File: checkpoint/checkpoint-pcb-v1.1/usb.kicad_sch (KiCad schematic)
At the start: 7 parts, among them J16 USB_C_Receptacle_USB2.0_16P, U4 USBLC6-2P6

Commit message: chore: reset refdes numbers
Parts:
- renumbered J16 to J17
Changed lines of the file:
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@@
 		(dnp no)
 		(fields_autoplaced yes)
-		(property "Reference" "#PWR049"
+		(property "Reference" "#PWR051"
 			(at 151.13 58.42 0)
 			(effects
@@
 			(project "checkpoint"
 				(path "/3a22685f-fb6f-4c54-b509-09f3e7d2168e/d0edb953-abc9-4de2-ace2-d042dedd6b65"
-					(reference "#PWR049")
+					(reference "#PWR051")
 					(unit 1)
 				)
@@
 		(dnp no)
 		(fields_autoplaced yes)
-		(property "Reference" "#PWR051"
+		(property "Reference" "#PWR053"
 			(at 199.39 152.4 0)
 			(effects
@@
 			(project "checkpoint"
 				(path "/3a22685f-fb6f-4c54-b509-09f3e7d2168e/d0edb953-abc9-4de2-ace2-d042dedd6b65"
-					(reference "#PWR051")
+					(reference "#PWR053")
 					(unit 1)
 				)
@@
 		(on_board yes)
 		(dnp no)
-		(property "Reference" "J16"
+		(property "Reference" "J17"
 			(at 135.89 108.458 0)
 			(effects
@@
 			(project "checkpoint"
 				(path "/3a22685f-fb6f-4c54-b509-09f3e7d2168e/d0edb953-abc9-4de2-ace2-d042dedd6b65"
-					(reference "J16")
+					(reference "J17")
 					(unit 1)
 				)
@@
 		(dnp no)
 		(fields_autoplaced yes)
-		(property "Reference" "#PWR050"
+		(property "Reference" "#PWR052"
 			(at 158.75 58.42 0)
 			(effects
@@
 			(project "checkpoint"
 				(path "/3a22685f-fb6f-4c54-b509-09f3e7d2168e/d0edb953-abc9-4de2-ace2-d042dedd6b65"
-					(reference "#PWR050")
+					(reference "#PWR052")
 					(unit 1)
 				)
@@
 		(dnp no)
 		(fields_autoplaced yes)
-		(property "Reference" "#PWR046"
+		(property "Reference" "#PWR048"
 			(at 110.49 130.81 0)
 			(effects
@@
 			(project "checkpoint"
 				(path "/3a22685f-fb6f-4c54-b509-09f3e7d2168e/d0edb953-abc9-4de2-ace2-d042dedd6b65"
-					(reference "#PWR046")
+					(reference "#PWR048")
 					(unit 1)
 				)
@@
 		(dnp no)
 		(fields_autoplaced yes)
-		(property "Reference" "#PWR048"
+		(property "Reference" "#PWR050"
 			(at 147.32 144.78 0)
 			(effects
@@
 			(project "checkpoint"
 				(path "/3a22685f-fb6f-4c54-b509-09f3e7d2168e/d0edb953-abc9-4de2-ace2-d042dedd6b65"
-					(reference "#PWR048")
+					(reference "#PWR050")
 					(unit 1)
 				)
@@
 		(dnp no)
 		(fields_autoplaced yes)
-		(property "Reference" "#PWR047"
+		(property "Reference" "#PWR049"
 			(at 118.11 97.79 0)
 			(effects
@@
 			(project "checkpoint"
 				(path "/3a22685f-fb6f-4c54-b509-09f3e7d2168e/d0edb953-abc9-4de2-ace2-d042dedd6b65"
-					(reference "#PWR047")
+					(reference "#PWR049")
 					(unit 1)
 				)

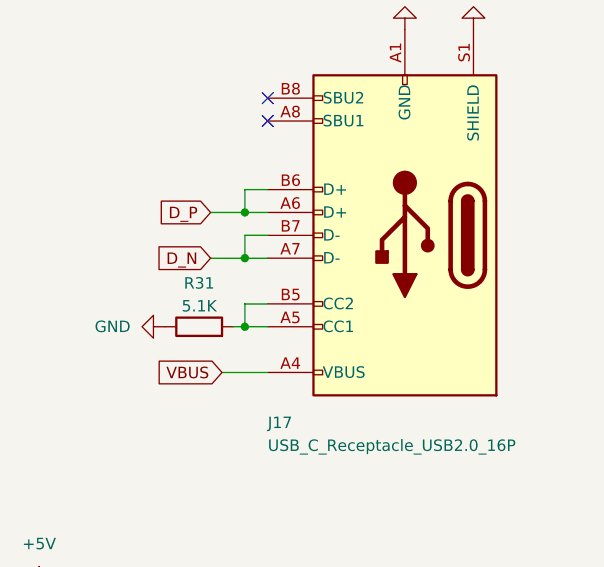
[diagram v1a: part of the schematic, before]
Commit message: fix: add i2c pullup resistors
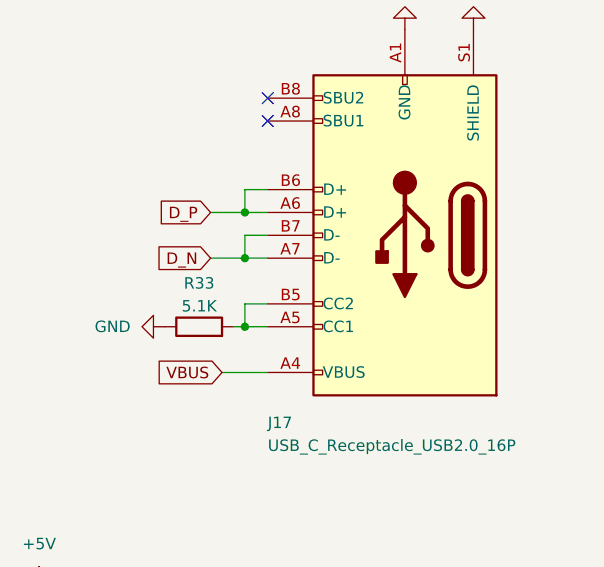
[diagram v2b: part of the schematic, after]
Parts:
- renumbered R31 to R33
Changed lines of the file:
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@@
 		(dnp no)
 		(fields_autoplaced yes)
-		(property "Reference" "#PWR051"
+		(property "Reference" "#PWR052"
 			(at 151.13 58.42 0)
 			(effects
@@
 			(project "checkpoint"
 				(path "/3a22685f-fb6f-4c54-b509-09f3e7d2168e/d0edb953-abc9-4de2-ace2-d042dedd6b65"
-					(reference "#PWR051")
+					(reference "#PWR052")
 					(unit 1)
 				)
@@
 		(dnp no)
 		(fields_autoplaced yes)
-		(property "Reference" "#PWR053"
+		(property "Reference" "#PWR054"
 			(at 199.39 152.4 0)
 			(effects
@@
 			(project "checkpoint"
 				(path "/3a22685f-fb6f-4c54-b509-09f3e7d2168e/d0edb953-abc9-4de2-ace2-d042dedd6b65"
-					(reference "#PWR053")
+					(reference "#PWR054")
 					(unit 1)
 				)
@@
 		(dnp no)
 		(fields_autoplaced yes)
-		(property "Reference" "#PWR052"
+		(property "Reference" "#PWR053"
 			(at 158.75 58.42 0)
 			(effects
@@
 			(project "checkpoint"
 				(path "/3a22685f-fb6f-4c54-b509-09f3e7d2168e/d0edb953-abc9-4de2-ace2-d042dedd6b65"
-					(reference "#PWR052")
+					(reference "#PWR053")
 					(unit 1)
 				)
@@
 		(dnp no)
 		(fields_autoplaced yes)
-		(property "Reference" "#PWR048"
+		(property "Reference" "#PWR049"
 			(at 110.49 130.81 0)
 			(effects
@@
 			(project "checkpoint"
 				(path "/3a22685f-fb6f-4c54-b509-09f3e7d2168e/d0edb953-abc9-4de2-ace2-d042dedd6b65"
-					(reference "#PWR048")
+					(reference "#PWR049")
 					(unit 1)
 				)
@@
 		(dnp no)
 		(fields_autoplaced yes)
-		(property "Reference" "#PWR050"
+		(property "Reference" "#PWR051"
 			(at 147.32 144.78 0)
 			(effects
@@
 			(project "checkpoint"
 				(path "/3a22685f-fb6f-4c54-b509-09f3e7d2168e/d0edb953-abc9-4de2-ace2-d042dedd6b65"
-					(reference "#PWR050")
+					(reference "#PWR051")
 					(unit 1)
 				)
@@
 		(dnp no)
 		(fields_autoplaced yes)
-		(property "Reference" "#PWR049"
+		(property "Reference" "#PWR050"
 			(at 118.11 97.79 0)
 			(effects
@@
 			(project "checkpoint"
 				(path "/3a22685f-fb6f-4c54-b509-09f3e7d2168e/d0edb953-abc9-4de2-ace2-d042dedd6b65"
-					(reference "#PWR049")
+					(reference "#PWR050")
 					(unit 1)
 				)
@@
 		(on_board yes)
 		(dnp no)
-		(property "Reference" "R31"
+		(property "Reference" "R33"
 			(at 128.27 92.964 90)
 			(effects
@@
 			(project "checkpoint"
 				(path "/3a22685f-fb6f-4c54-b509-09f3e7d2168e/d0edb953-abc9-4de2-ace2-d042dedd6b65"
-					(reference "R31")
+					(reference "R33")
 					(unit 1)
 				)

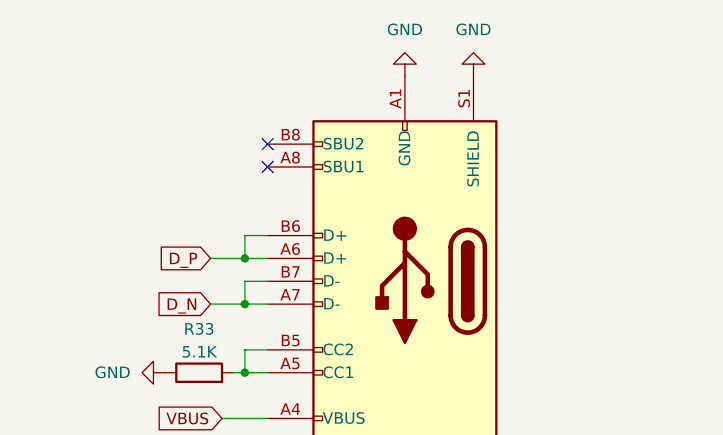
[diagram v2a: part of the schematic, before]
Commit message: chore: switch to vertical usb-c port
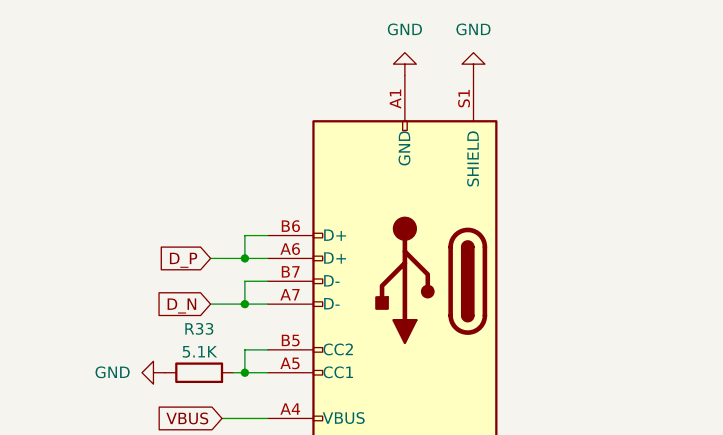
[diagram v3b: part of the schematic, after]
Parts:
- J17: footprint Connector_USB:USB_C_Receptacle_XKB_U262-16XN-4BVC11 -> Library:USB_C_14P_VERT_XUNPU; symbol Connector:USB_C_Receptacle_USB2.0_16P -> Connector:USB_C_Receptacle_USB2.0_14P
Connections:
- no-connect marks 2 -> 0
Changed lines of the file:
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@@
 		(color 0 0 0 0)
-	)
-	(no_connect
-		(at 135.89 72.39)
-	)
-	(no_connect
-		(at 135.89 74.93)
 	)
 	(wire
@@
 	)
 	(symbol
-		(lib_id "Connector:USB_C_Receptacle_USB2.0_16P")
+		(lib_id "Connector:USB_C_Receptacle_USB2.0_14P")
 		(at 151.13 87.63 180)
 		(unit 1)
@@
 			)
 		)
-		(property "Footprint" "Connector_USB:USB_C_Receptacle_XKB_U262-16XN-4BVC11"
+		(property "Footprint" "Library:USB_C_14P_VERT_XUNPU"
 			(at 147.32 87.63 0)
 			(effects
@@
 			)
 		)
-		(property "Description" "USB 2.0-only 16P Type-C Receptacle connector"
+		(property "Description" "USB 2.0-only 14P Type-C Receptacle connector"
 			(at 151.13 87.63 0)
 			(effects
@@
 		(pin "A9"
 		)
-		(pin "A8"
-		)
-		(pin "B8"
-		)
 		(instances

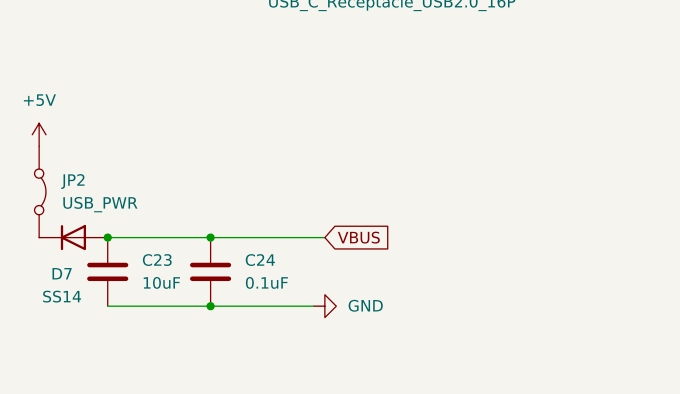
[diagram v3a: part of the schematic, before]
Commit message: chore: update component rotation
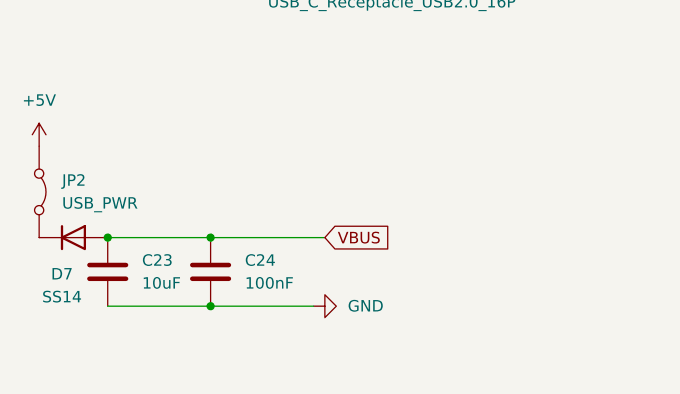
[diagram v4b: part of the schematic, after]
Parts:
- C24: value 0.1uF -> 100nF
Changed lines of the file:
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@@
 			)
 		)
-		(property "Value" "0.1uF"
+		(property "Value" "100nF"
 			(at 133.35 142.2399 0)
 			(effects
